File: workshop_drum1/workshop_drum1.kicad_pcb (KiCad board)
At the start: 2 copper layers, 62.2 x 45 mm, 40 parts, among them J1 9v_Battery_Clip, J2 Trigger_Input, J3 Output, U1 LM358, U2 7414, U3 78L05

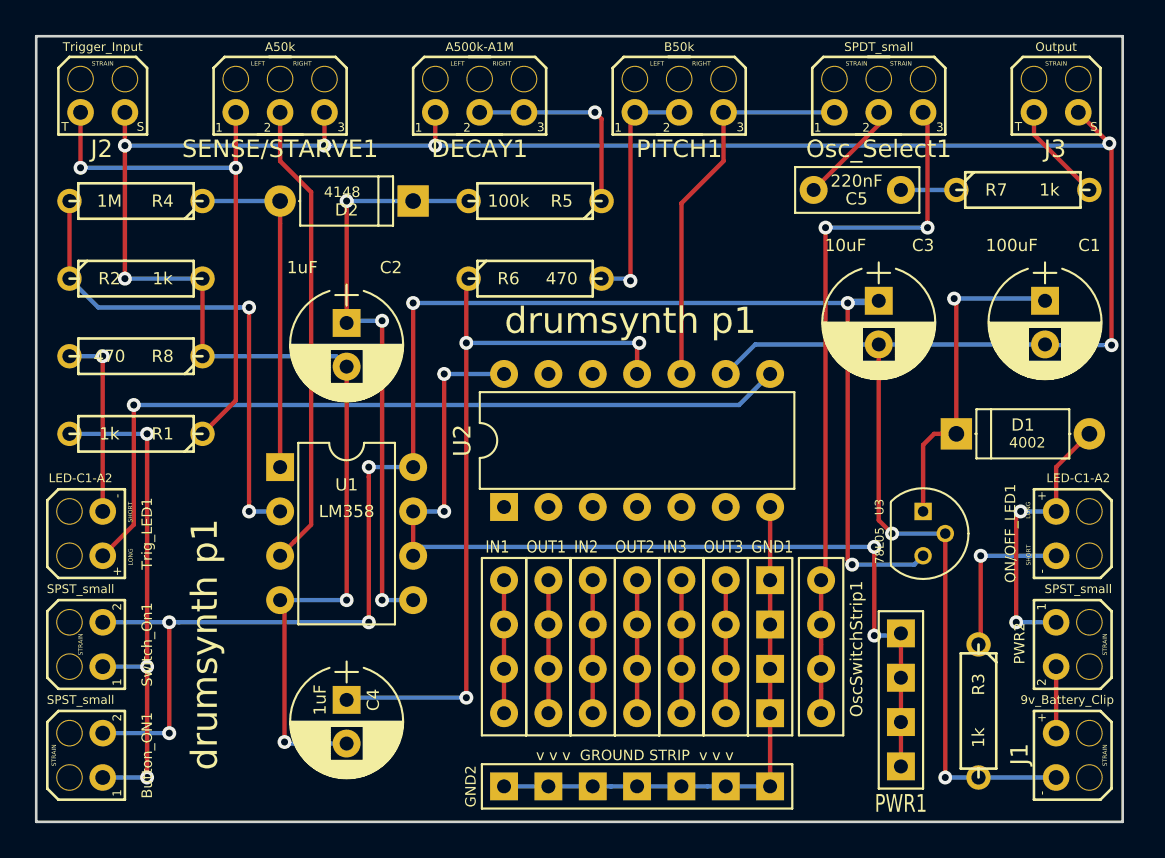
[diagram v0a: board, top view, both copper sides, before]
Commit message: got rid of square pins - printed gerbers - changed names- relayed traces
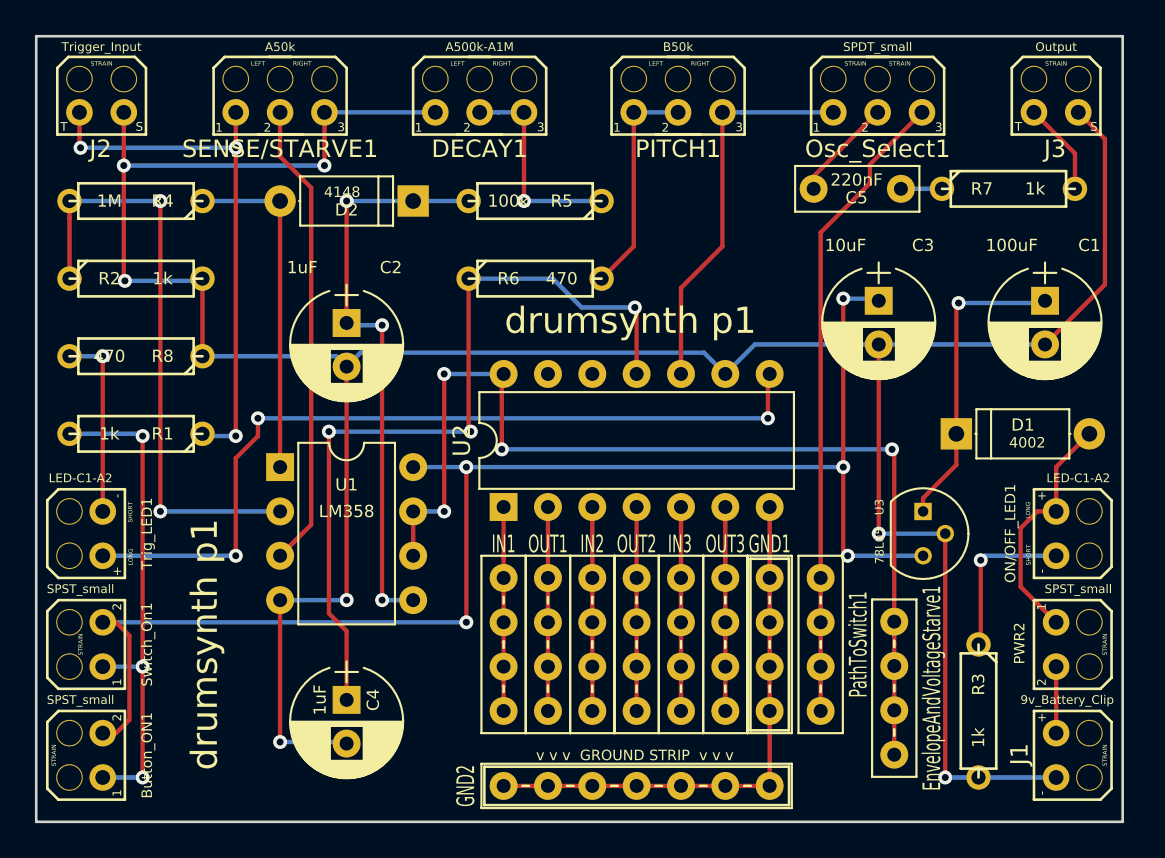
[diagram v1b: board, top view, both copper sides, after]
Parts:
- removed OscSwitchStrip1: BreadBoardStrip, zfoot:BreadBoardStrip
- removed PWR1: PWRStrip, zfoot:GNDStrip
- added EnvelopeAndVoltageStarve1: PWRStrip, zfoot:BreadBoardStrip_4, F.Cu at (49.1, -7.66)
- added PathToSwitch1: BreadBoardStrip, zfoot:BreadBoardStrip_4, F.Cu at (44.9, -10.2)
- GND1: footprint zfoot:GNDStrip -> zfoot:BreadBoardStripBold_4
- GND2: footprint zfoot:GNDStripLONG -> zfoot:BreadBoardStripBold_7
- IN1, IN2, IN3, OUT1, OUT2, OUT3: footprint zfoot:BreadBoardStrip -> zfoot:BreadBoardStrip_4
- moved GND2 7.59 mm to (34.4, -2.06)
- moved GND1 3.68 mm to (42.0, -10.2)
- moved IN1 3.68 mm to (26.8, -10.2)
- moved IN2 3.68 mm to (31.9, -10.2)
- moved IN3 3.68 mm to (36.9, -10.2)
- moved OUT1 3.68 mm to (29.3, -10.2)
- moved OUT2 3.68 mm to (34.4, -10.2)
- moved OUT3 3.68 mm to (39.5, -10.2)
- moved R7 0.83 mm to (55.7, -36.3)
- moved J2 0.06 mm to (3.75, -40.6)
- moved C5 0.06 mm to (49.5, -36.3)
- moved Osc_Select1 0.06 mm to (48.2, -40.6)
- moved PITCH1 0.06 mm to (36.8, -40.6)
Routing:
- net GND: track 187.8 -> 169.0 mm, vias 10 -> 7
- net +5V: track 94.0 -> 84.1 mm, vias 7 -> 5
- net Net-(R2-Pad1): track 28.9 -> 34.3 mm
- net Net-(C4-Pad1): track 42.7 -> 46.8 mm
- net Net-(OUT3-Pad1): track 7.62 -> 11.7 mm
- net Net-(OUT2-Pad1): track 7.62 -> 11.7 mm
- net Net-(OUT1-Pad1): track 7.62 -> 11.7 mm
- net Net-(IN3-Pad1): track 7.62 -> 11.7 mm
- net Net-(IN2-Pad1): track 7.62 -> 11.7 mm
- net Net-(IN1-Pad1): track 7.62 -> 11.7 mm
- net Net-(Osc_Select1-Pad3): track 40.5 -> 36.7 mm, vias 2 -> 0
- net Net-(EnvelopeAndVoltageStarve1-Pad1): track 56.5 -> 60.0 mm
- net Net-(D1-Pad2): track 16.0 -> 13.9 mm, vias 2 -> 0
- net Net-(Trig_LED1-Pad2): track 46.6 -> 47.8 mm, vias 1 -> 3
- net Net-(C1-Pad1): track 19.0 -> 17.8 mm
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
